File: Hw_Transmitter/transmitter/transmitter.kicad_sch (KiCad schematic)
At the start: 18 parts, among them SW1 SW_SPDT, SW2 toggle switch, U1 BP, U2 nRF24L01+, U3 left joystick, U4 right joystick, U6 ams1117, U7 left joystick mounting, U8 right joystick mounting

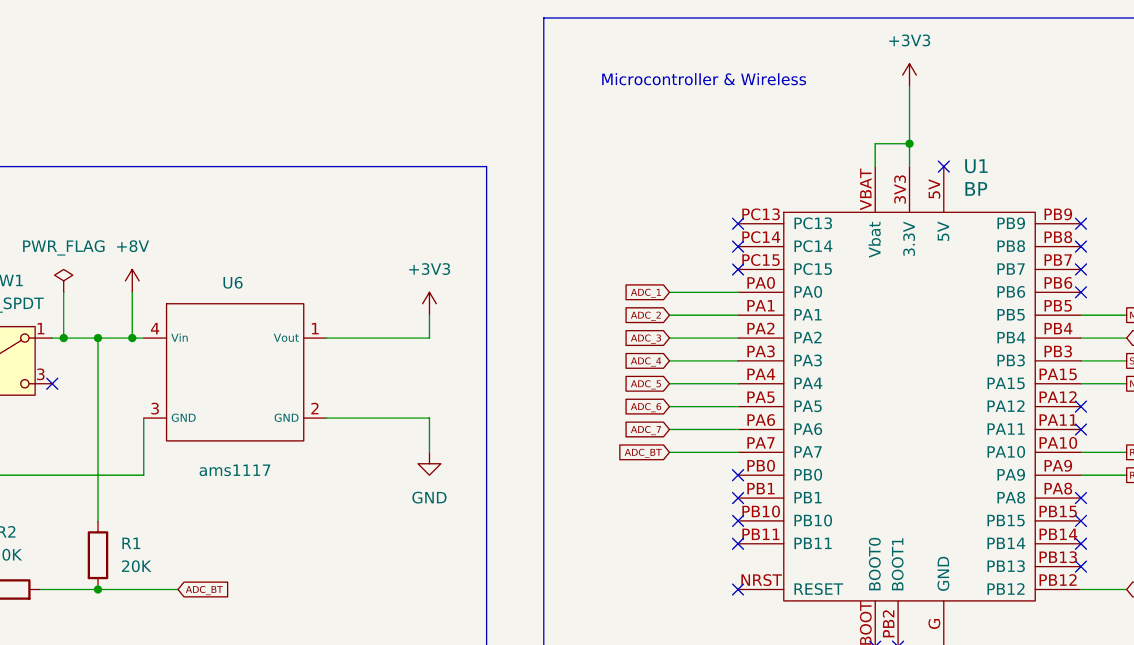
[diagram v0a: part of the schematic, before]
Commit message: 1. transmitter: replace ams1117-3.3V with ams1117-5V. 2. remove backup files and update git ignore file.
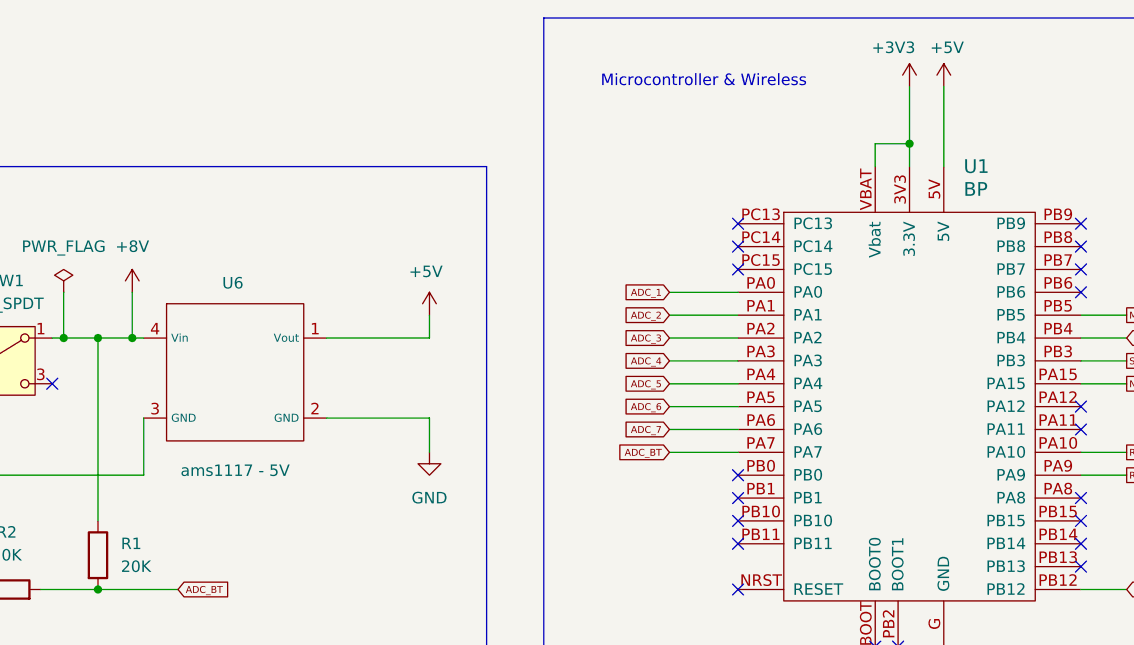
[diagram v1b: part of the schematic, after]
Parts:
- U6: value ams1117 -> ams1117 - 5V
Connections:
- net +3V3: no longer U6.1 (Vout)
- net +5V: now reaches U1.5V
- net +5V: now also U6.1 (Vout)
- no-connect marks 22 -> 21
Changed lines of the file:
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@@
 	)
 	(no_connect
-		(at 144.78 33.02)
-	)
-	(no_connect
 		(at 160.02 39.37)
 	)
@@
 	(wire
 		(pts
+			(xy 144.78 24.13) (xy 144.78 33.02)
+		)
+		(stroke
+			(width 0)
+			(type default)
+		)
+	)
+	(wire
+		(pts
 			(xy 25.4 57.15) (xy 25.4 54.61)
 		)
@@
 	)
 	(symbol
+		(lib_id "power:+3V3")
+		(at 144.78 24.13 0)
+		(unit 1)
+		(exclude_from_sim no)
+		(in_bom yes)
+		(on_board yes)
+		(dnp no)
+		(property "Reference" "#PWR011"
+			(at 144.78 27.94 0)
+			(effects
+				(font
+					(size 1.27 1.27)
+				)
+				(hide yes)
+			)
+		)
+		(property "Value" "+5V"
+			(at 143.256 19.812 0)
+			(effects
+				(font
+					(size 1.27 1.27)
+				)
+				(justify left)
+			)
+		)
+		(property "Footprint" ""
+			(at 144.78 24.13 0)
+			(effects
+				(font
+					(size 1.27 1.27)
+				)
+				(hide yes)
+			)
+		)
+		(property "Datasheet" ""
+			(at 144.78 24.13 0)
+			(effects
+				(font
+					(size 1.27 1.27)
+				)
+				(hide yes)
+			)
+		)
+		(property "Description" "Power symbol creates a global label with name \"+3V3\""
+			(at 144.78 24.13 0)
+			(effects
+				(font
+					(size 1.27 1.27)
+				)
+				(hide yes)
+			)
+		)
+		(pin "1"
+		)
+		(instances
+			(project "transmitter"
+				(path "/db82cf10-392f-4771-a2c5-0f7ef88c3a96"
+					(reference "#PWR011")
+					(unit 1)
+				)
+			)
+		)
+	)
+	(symbol
 		(lib_id "nRF24L01+:nRF24L01+")
 		(at 234.95 60.96 0)
@@
 			)
 		)
-		(property "Value" "ams1117"
+		(property "Value" "ams1117 - 5V"
 			(at 66.04 66.802 0)
 			(effects
@@
 		(on_board yes)
 		(dnp no)
-		(fields_autoplaced yes)
 		(property "Reference" "#PWR03"
 			(at 87.63 53.34 0)
@@
 			)
 		)
-		(property "Value" "+3V3"
-			(at 87.63 44.45 0)
+		(property "Value" "+5V"
+			(at 85.344 44.704 0)
 			(effects
 				(font
 					(size 1.27 1.27)
 				)
+				(justify left)
 			)
 		)
@@
 		(on_board yes)
 		(dnp no)
-		(fields_autoplaced yes)
 		(property "Reference" "#PWR06"
 			(at 140.97 27.94 0)
@@
 		)
 		(property "Value" "+3V3"
-			(at 140.97 19.05 0)
+			(at 139.192 19.812 0)
 			(effects
 				(font
